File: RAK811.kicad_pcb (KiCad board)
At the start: 2 copper layers, 27.5 x 46.5 mm, 51 parts, among them J1 CONN_01X01, P1 CONN_01X02, P2 CONN_01X03, P3 CONN_01X06, P4 CONN_01X15, P5 CONN_01X15, P6 CONN_01X02, SW1 SW_SPST_Small, U1 RAK811, U2 LD1117S12CTR

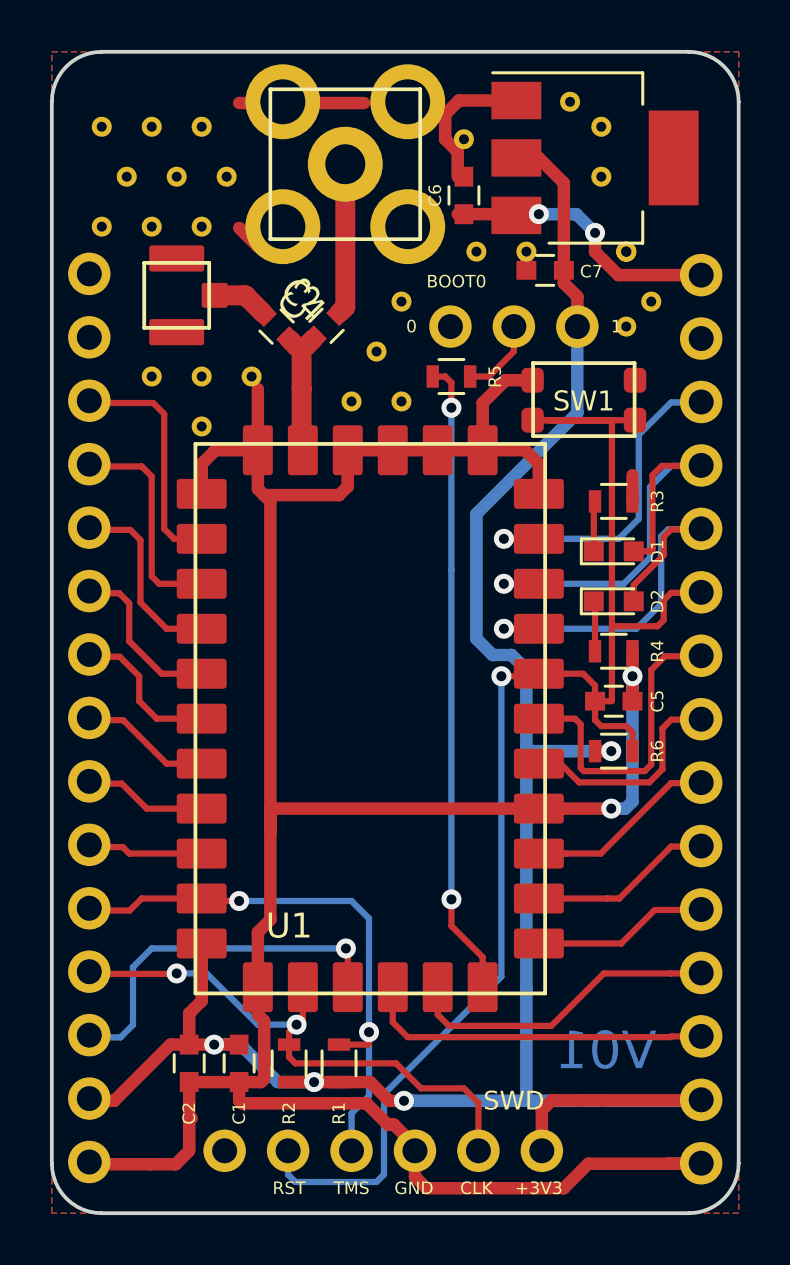
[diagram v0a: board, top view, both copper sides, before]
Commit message: rak811_breakout: Update to V2.1
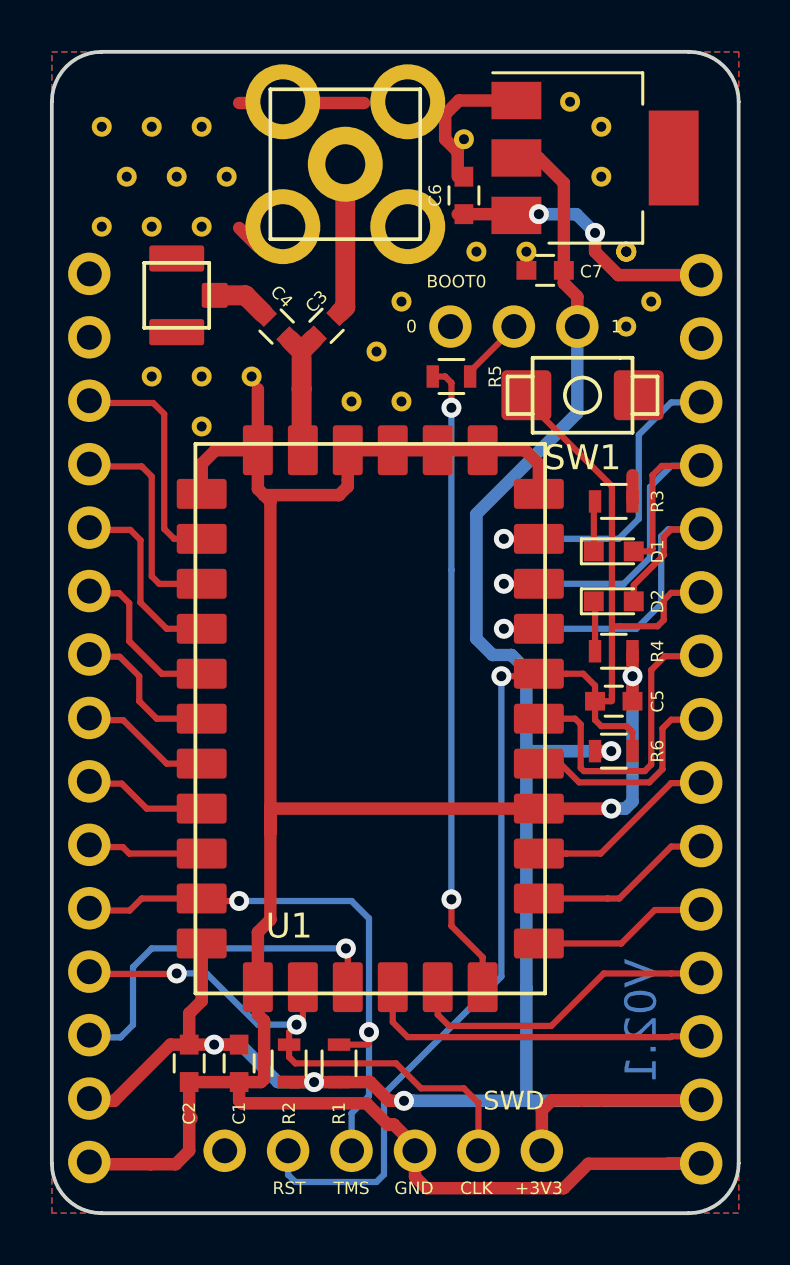
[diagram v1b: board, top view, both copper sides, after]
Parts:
- SW1: footprint KMR241NG:KMR241NG -> tactile_button:3X4MM Tactile Tact Push Button
- moved SW1 1.00 mm to (70.2, 52.8)
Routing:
- net RST: track 61.5 -> 54.0 mm
- net GND: track 119.3 -> 115.0 mm
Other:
- board text added: "V02.1"
- board text removed: "V01"
